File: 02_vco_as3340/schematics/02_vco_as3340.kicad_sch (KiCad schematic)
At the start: 87 parts, among them J1 Conn_02x05_Odd_Even, J10 Triangle Out, J11 Sine Out, J12 1V/O Thru, J2 1V/O IN, J3 Positive Hard Sync IN, J4 Negative Hard Sync IN, J5 Soft Sync In, J6 FM IN, J7 PWM CV IN, J8 Square Out, J9 Sawtooth Out, Q1 2N3904, Q2 2N3904, U1 TL074, U2 AS3340, U3 TL072

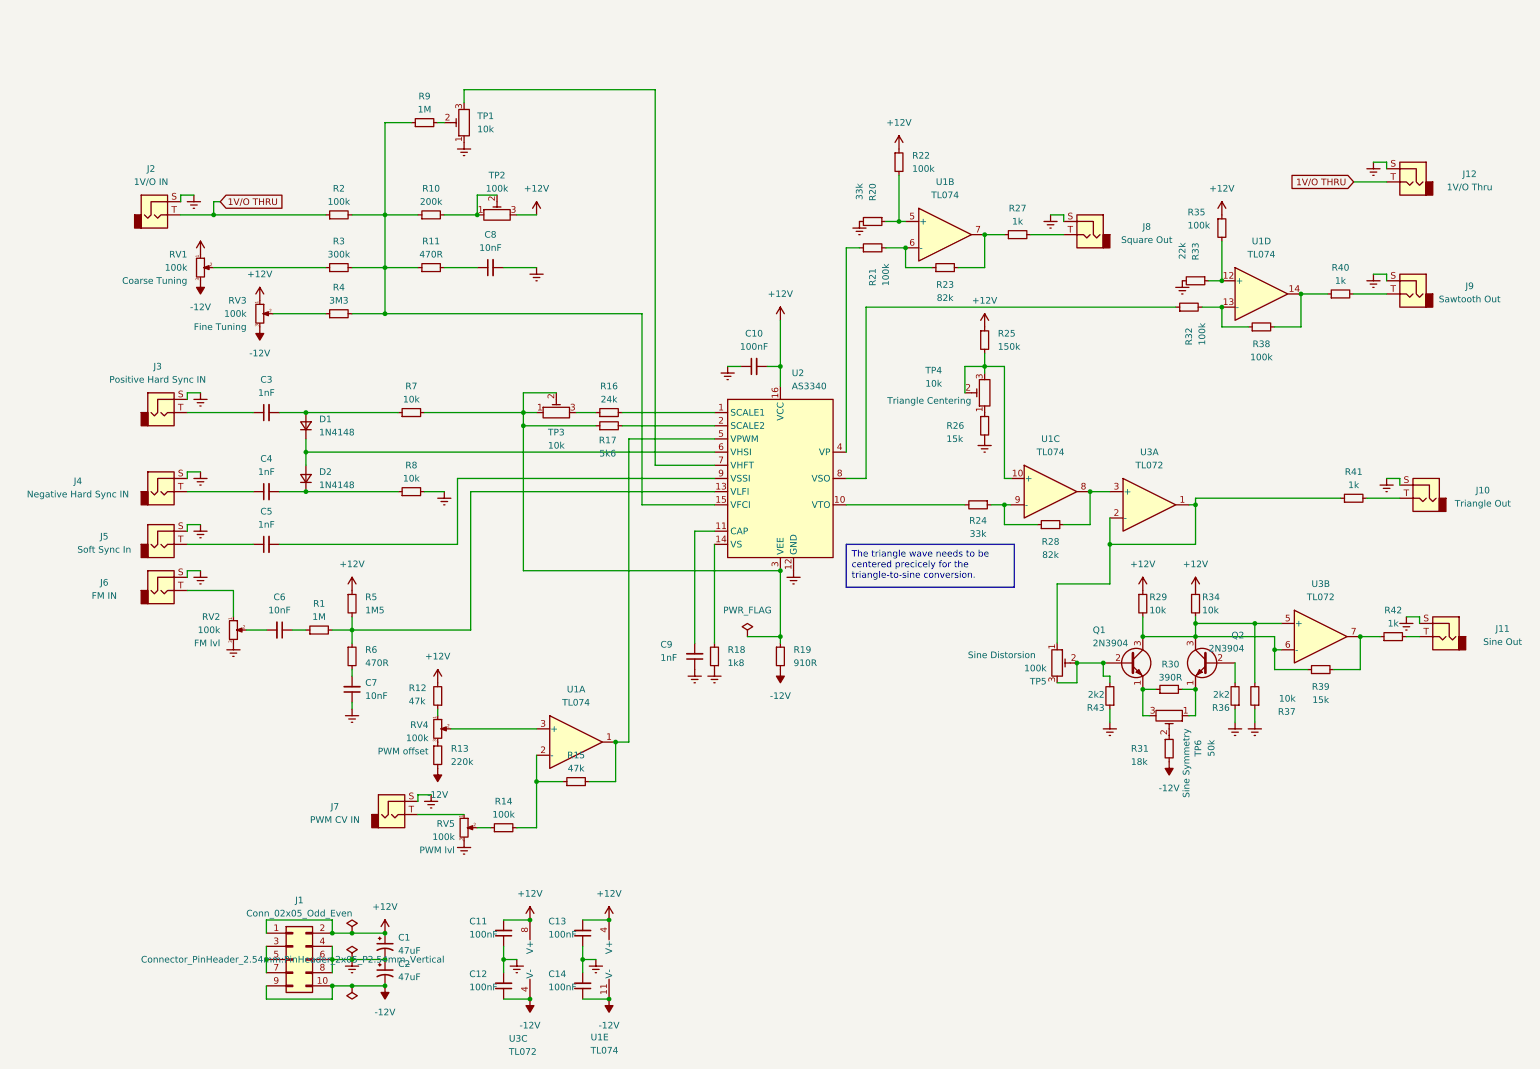
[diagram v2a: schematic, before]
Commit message: added stripboard for 3340 vco
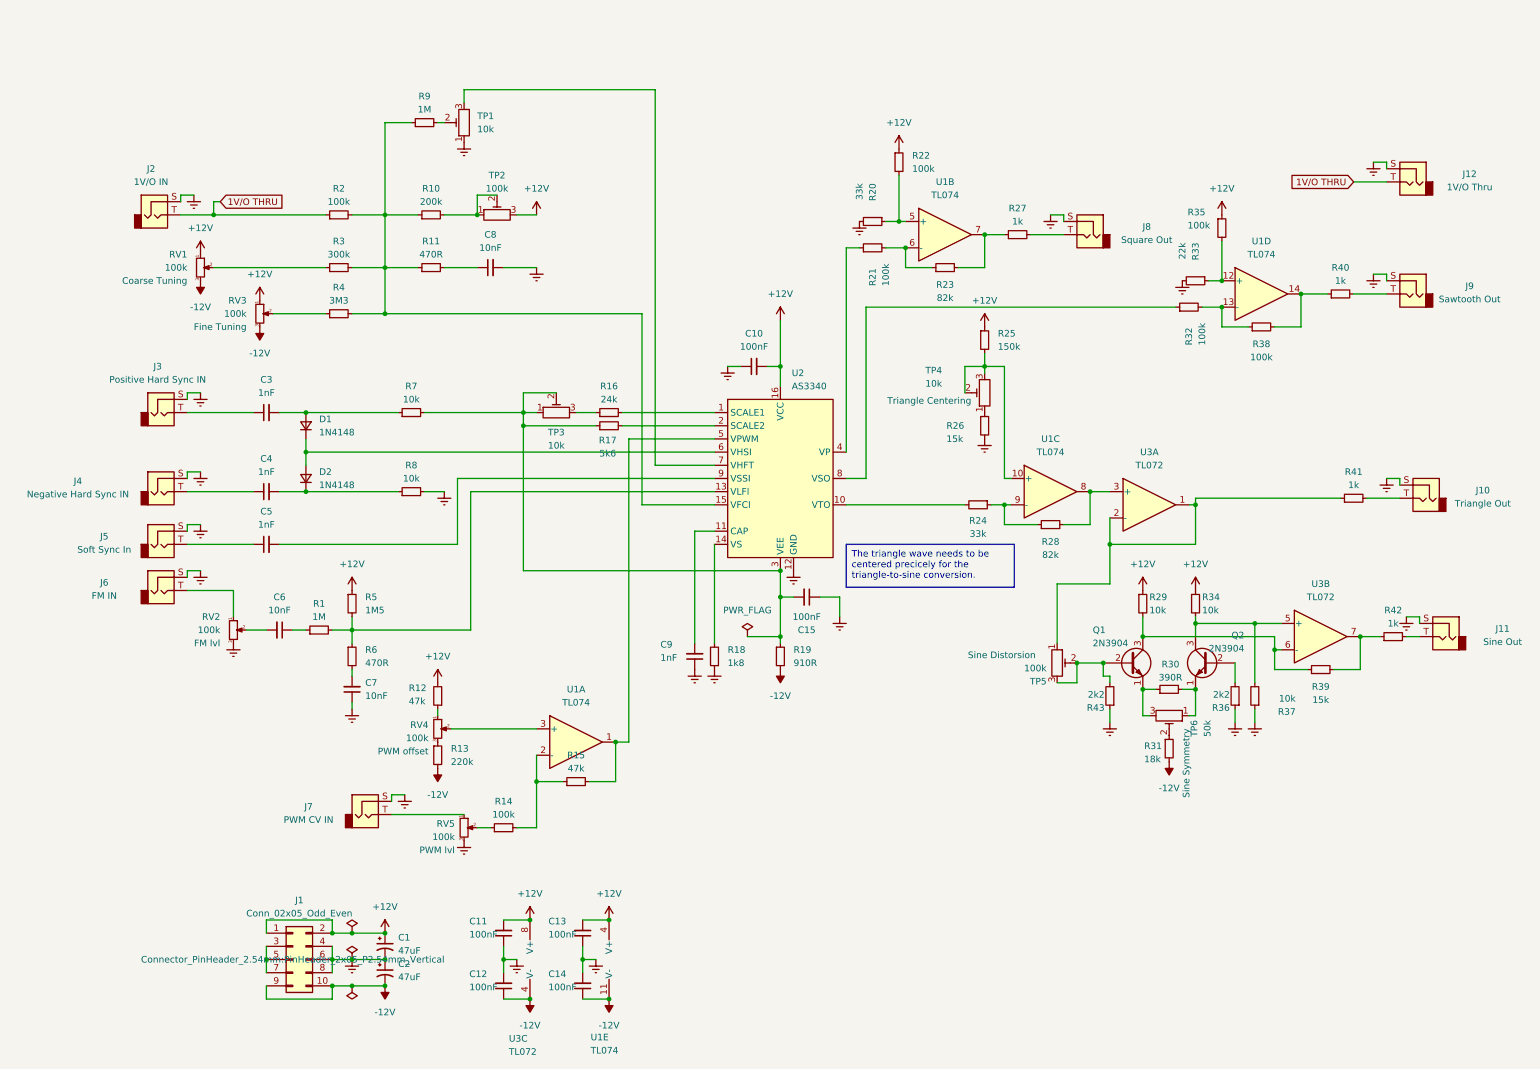
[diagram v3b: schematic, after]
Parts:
- added C15: 100nF, Capacitor_THT:C_Disc_D6.0mm_W2.5mm_P5.00mm, symbol Device:C_Small
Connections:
- net GNDREF: now also C15.1
- net at R17.1, R19.1, R7.2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: now also C15.2
- net at Q1.3 (C), R29.2, R39.1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: no longer Q2.3 (C), R34.2, R37.2, U3.5 (+)
- new net: Q2.3 (C), R34.2, R37.2, U3.5 (+)
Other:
- moved on the sheet: J7
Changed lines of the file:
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@@
 	)
 	(junction
-		(at 223.52 133.35)
-		(diameter 0)
-		(color 0 0 0 0)
-	)
-	(junction
 		(at 67.31 200.66)
 		(diameter 0)
@@
 	)
 	(junction
+		(at 143.51 125.73)
+		(diameter 0)
+		(color 0 0 0 0)
+	)
+	(junction
 		(at 234.95 130.81)
 		(diameter 0)
@@
 	(wire
 		(pts
-			(xy 213.36 133.35) (xy 223.52 133.35)
-		)
-		(stroke
-			(width 0)
-			(type default)
-		)
-	)
-	(wire
-		(pts
 			(xy 187.96 107.95) (xy 186.69 107.95)
 		)
@@
 	(wire
 		(pts
+			(xy 146.05 125.73) (xy 143.51 125.73)
+		)
+		(stroke
+			(width 0)
+			(type default)
+		)
+	)
+	(wire
+		(pts
 			(xy 228.6 69.85) (xy 228.6 73.66)
 		)
@@
 	(wire
 		(pts
-			(xy 73.66 167.64) (xy 82.55 167.64)
+			(xy 68.58 167.64) (xy 82.55 167.64)
 		)
 		(stroke
@@
 	(wire
 		(pts
-			(xy 223.52 133.35) (xy 238.76 133.35)
+			(xy 213.36 133.35) (xy 238.76 133.35)
 		)
 		(stroke
@@
 	(wire
 		(pts
+			(xy 154.94 125.73) (xy 154.94 129.54)
+		)
+		(stroke
+			(width 0)
+			(type default)
+		)
+	)
+	(wire
+		(pts
 			(xy 60.96 190.5) (xy 67.31 190.5)
 		)
@@
 	(wire
 		(pts
-			(xy 73.66 163.83) (xy 73.66 165.1)
+			(xy 68.58 163.83) (xy 68.58 165.1)
 		)
 		(stroke
@@
 	(wire
 		(pts
+			(xy 154.94 125.73) (xy 151.13 125.73)
+		)
+		(stroke
+			(width 0)
+			(type default)
+		)
+	)
+	(wire
+		(pts
 			(xy 240.03 135.89) (xy 238.76 135.89)
 		)
@@
 	(wire
 		(pts
-			(xy 76.2 163.83) (xy 73.66 163.83)
+			(xy 71.12 163.83) (xy 68.58 163.83)
 		)
 		(stroke
@@
 	(wire
 		(pts
-			(xy 143.51 120.65) (xy 143.51 133.35)
+			(xy 143.51 120.65) (xy 143.51 125.73)
 		)
 		(stroke
@@
 	(wire
 		(pts
+			(xy 143.51 125.73) (xy 143.51 133.35)
+		)
+		(stroke
+			(width 0)
+			(type default)
+		)
+	)
+	(wire
+		(pts
 			(xy 78.74 34.29) (xy 77.47 34.29)
 		)
@@
 	(symbol
 		(lib_id "Connector_Audio:AudioJack2")
-		(at 68.58 167.64 0)
+		(at 63.5 167.64 0)
 		(unit 1)
 		(exclude_from_sim no)
@@
 		(dnp no)
 		(property "Reference" "J7"
-			(at 57.658 166.116 0)
+			(at 52.578 166.116 0)
 			(effects
 				(font
@@
 		)
 		(property "Value" "PWM CV IN"
-			(at 57.658 168.656 0)
+			(at 52.578 168.656 0)
 			(effects
 				(font
@@
 		)
 		(property "Footprint" "Connector_Audio:Jack_6.35mm_Neutrik_NJ5FD-V_Vertical"
-			(at 68.58 167.64 0)
+			(at 63.5 167.64 0)
 			(effects
 				(font
@@
 		)
 		(property "Datasheet" "~"
-			(at 68.58 167.64 0)
+			(at 63.5 167.64 0)
 			(effects
 				(font
@@
 		)
 		(property "Description" ""
-			(at 68.58 167.64 0)
+			(at 63.5 167.64 0)
 			(effects
 				(font
@@
 					(size 1.27 1.27)
 				)
-				(hide yes)
 			)
 		)
@@
 		(dnp no)
 		(property "Reference" "TP6"
-			(at 224.028 156.464 0)
+			(at 223.266 152.654 0)
 			(effects
 				(font
@@
 		)
 		(property "Value" "50k"
-			(at 226.568 156.464 0)
+			(at 225.806 152.654 0)
 			(effects
 				(font
@@
 	)
 	(symbol
+		(lib_id "power:GNDREF")
+		(at 154.94 129.54 0)
+		(unit 1)
+		(exclude_from_sim no)
+		(in_bom yes)
+		(on_board yes)
+		(dnp no)
+		(fields_autoplaced yes)
+		(property "Reference" "#PWR053"
+			(at 154.94 135.89 0)
+			(effects
+				(font
+					(size 1.27 1.27)
+				)
+				(hide yes)
+			)
+		)
+		(property "Value" "GNDREF"
+			(at 154.94 134.62 0)
+			(effects
+				(font
+					(size 1.27 1.27)
+				)
+				(hide yes)
+			)
+		)
+		(property "Footprint" ""
+			(at 154.94 129.54 0)
+			(effects
+				(font
+					(size 1.27 1.27)
+				)
+				(hide yes)
+			)
+		)
+		(property "Datasheet" ""
+			(at 154.94 129.54 0)
+			(effects
+				(font
+					(size 1.27 1.27)
+				)
+				(hide yes)
+			)
+		)
+		(property "Description" "Power symbol creates a global label with name \"GNDREF\" , reference supply ground"
+			(at 154.94 129.54 0)
+			(effects
+				(font
+					(size 1.27 1.27)
+				)
+				(hide yes)
+			)
+		)
+		(pin "1"
+		)
+		(instances
+			(project "02_vco_as3340"
+				(path "/7bf3d2ed-8bab-4c92-b1a7-3c419691fd96"
+					(reference "#PWR053")
+					(unit 1)
+				)
+			)
+		)
+	)
+	(symbol
 		(lib_id "Device:C_Small")
 		(at 46.99 132.08 270)
@@
 	)
 	(symbol
+		(lib_id "Device:C_Small")
+		(at 148.59 125.73 270)
+		(unit 1)
+		(exclude_from_sim no)
+		(in_bom yes)
+		(on_board yes)
+		(dnp no)
+		(fields_autoplaced yes)
+		(property "Reference" "C15"
+			(at 148.5837 132.08 90)
+			(effects
+				(font
+					(size 1.27 1.27)
+				)
+			)
+		)
+		(property "Value" "100nF"
+			(at 148.5837 129.54 90)
+			(effects
+				(font
+					(size 1.27 1.27)
+				)
+			)
+		)
+		(property "Footprint" "Capacitor_THT:C_Disc_D6.0mm_W2.5mm_P5.00mm"
+			(at 148.59 125.73 0)
+			(effects
+				(font
+					(size 1.27 1.27)
+				)
+				(hide yes)
+			)
+		)
+		(property "Datasheet" "~"
+			(at 148.59 125.73 0)
+			(effects
+				(font
+					(size 1.27 1.27)
+				)
+				(hide yes)
+			)
+		)
+		(property "Description" "Unpolarized capacitor, small symbol"
+			(at 148.59 125.73 0)
+			(effects
+				(font
+					(size 1.27 1.27)
+				)
+				(hide yes)
+			)
+		)
+		(pin "2"
+		)
+		(pin "1"
+		)
+		(instances
+			(project "02_vco_as3340"
+				(path "/7bf3d2ed-8bab-4c92-b1a7-3c419691fd96"
+					(reference "C15")
+					(unit 1)
+				)
+			)
+		)
+	)
+	(symbol
 		(lib_id "power:GNDREF")
 		(at 31.75 86.36 0)
@@
 		(dnp no)
 		(property "Reference" "R31"
-			(at 211.074 154.94 0)
+			(at 213.614 154.432 0)
 			(effects
 				(font
@@
 		)
 		(property "Value" "18k"
-			(at 211.074 157.48 0)
+			(at 213.614 156.972 0)
 			(effects
 				(font
@@
 	(symbol
 		(lib_id "power:GNDREF")
-		(at 76.2 163.83 0)
+		(at 71.12 163.83 0)
 		(unit 1)
 		(exclude_from_sim no)
@@
 		(fields_autoplaced yes)
 		(property "Reference" "#PWR016"
-			(at 76.2 170.18 0)
+			(at 71.12 170.18 0)
 			(effects
 				(font
@@
 		)
 		(property "Value" "GNDREF"
-			(at 76.2 168.91 0)
+			(at 71.12 168.91 0)
 			(effects
 				(font
@@
 		)
 		(property "Footprint" ""
-			(at 76.2 163.83 0)
+			(at 71.12 163.83 0)
 			(effects
 				(font
@@
 		)
 		(property "Datasheet" ""
-			(at 76.2 163.83 0)
+			(at 71.12 163.83 0)
 			(effects
 				(font
@@
 		)
 		(property "Description" "Power symbol creates a global label with name \"GNDREF\" , reference supply ground"
-			(at 76.2 163.83 0)
+			(at 71.12 163.83 0)
 			(effects
 				(font
